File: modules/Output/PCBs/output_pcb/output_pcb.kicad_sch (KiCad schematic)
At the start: 12 parts, among them J10 Eurorack_2x5_Power, J11 Conn_01x03_Socket, J12 Conn_01x10_Socket, J3 ACJS-MV-3, J4 ACJS-MV-3, J5 ACJS-MV-3, J6 Conn_01x10_Pin, J7 Conn_01x10_Pin, J8 Conn_01x10_Pin, J9 Conn_01x10_Pin

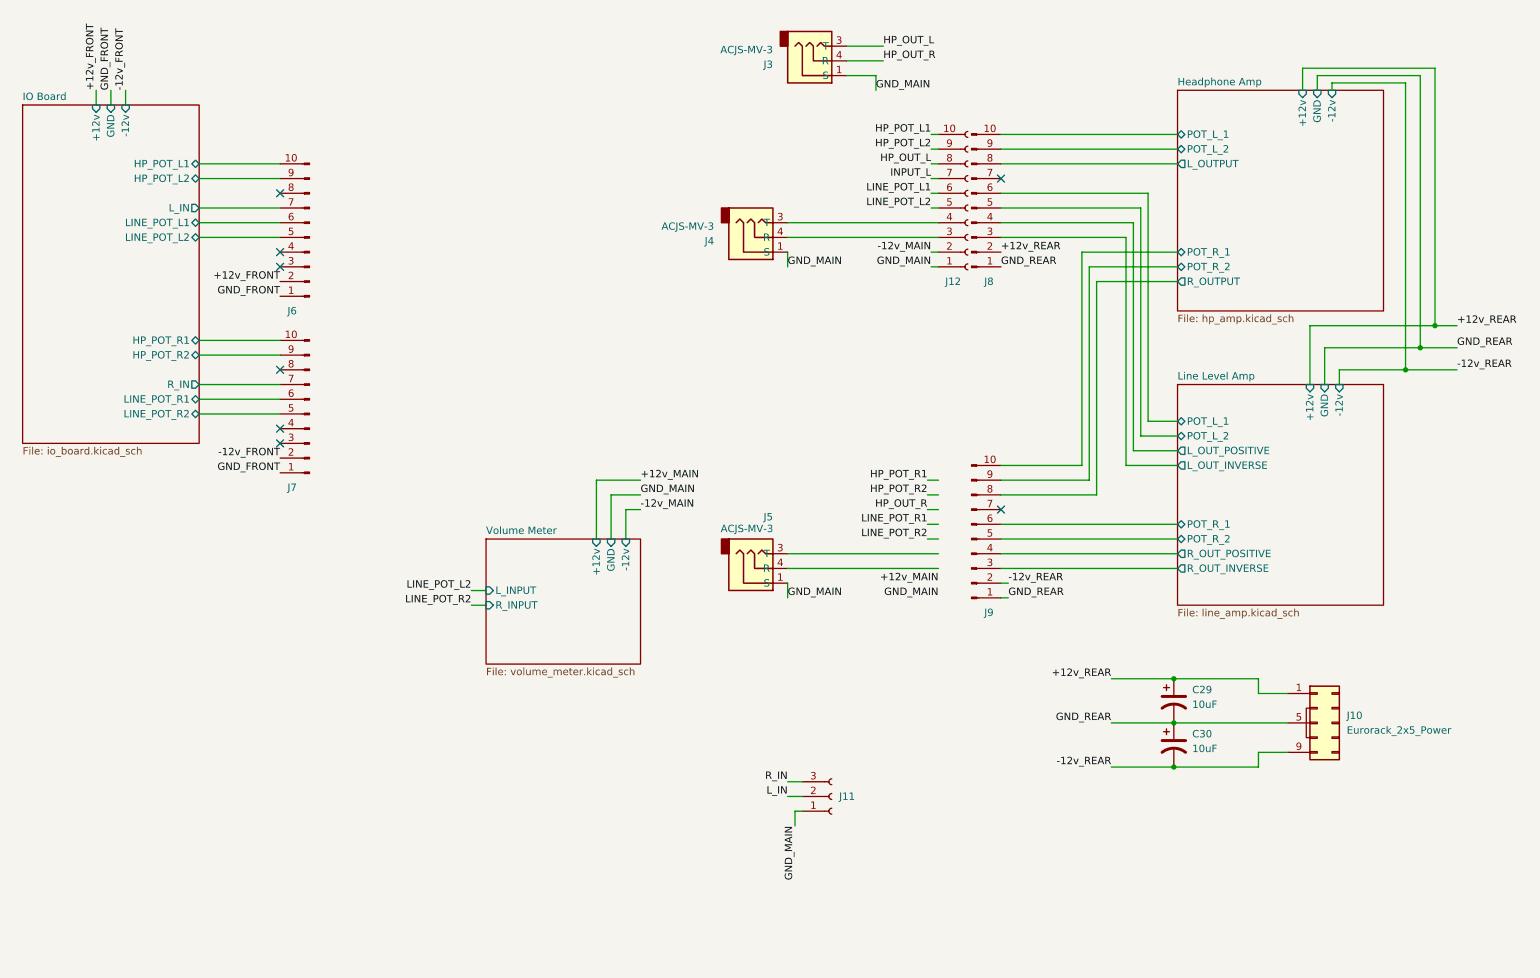
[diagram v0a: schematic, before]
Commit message: finish output PCB
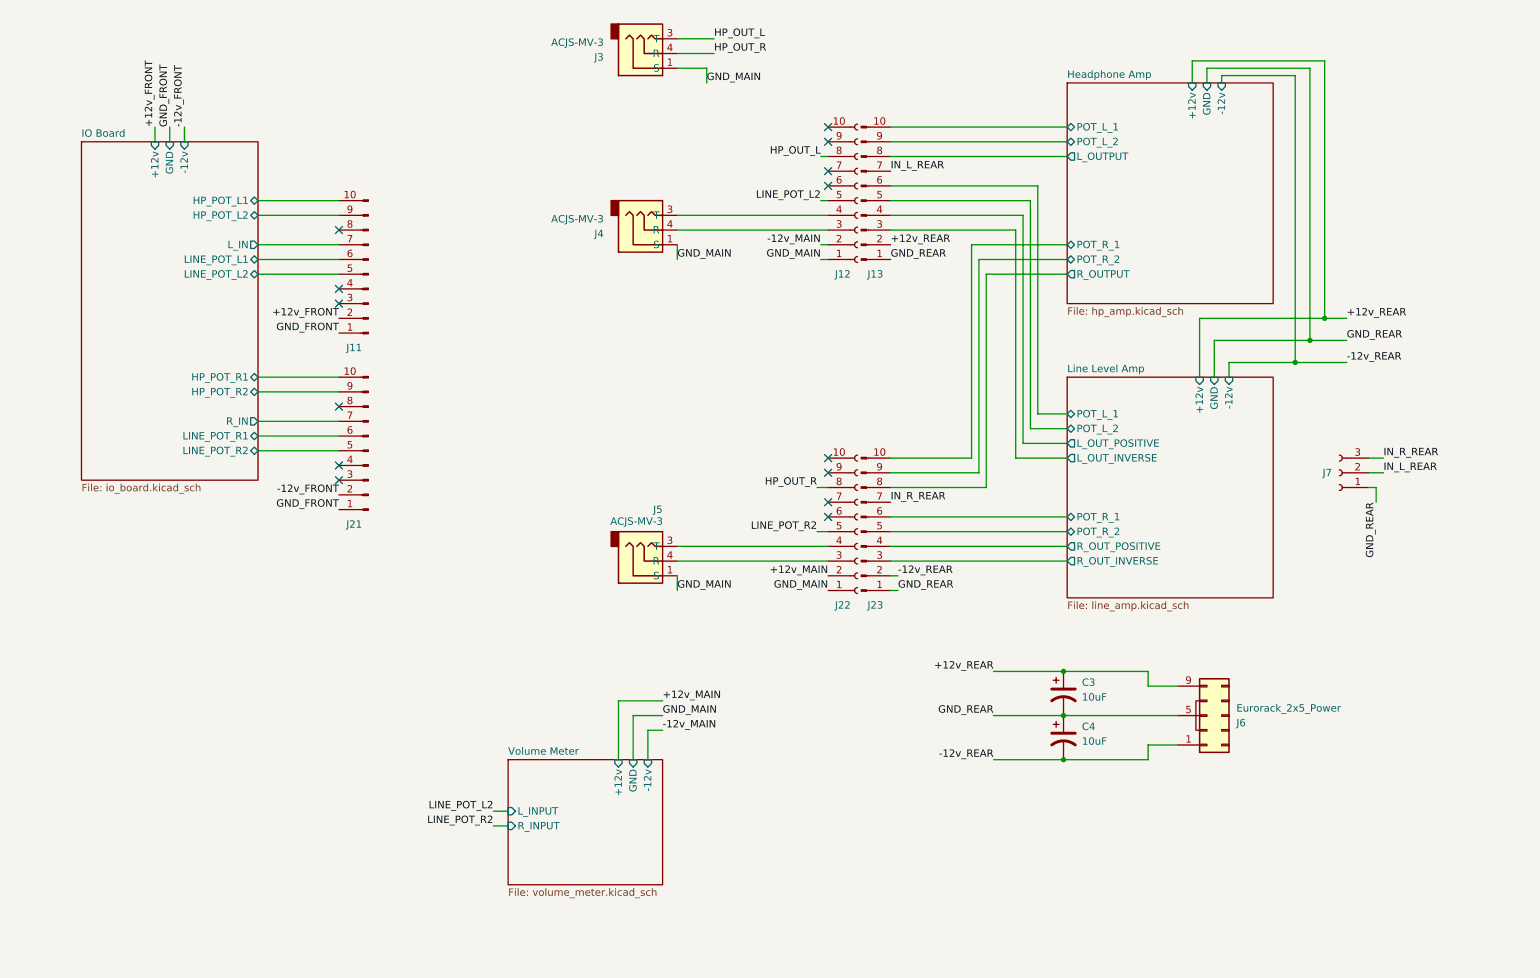
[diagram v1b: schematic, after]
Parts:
- added J22: Conn_01x10_Socket, Connector_PinHeader_2.54mm:PinHeader_1x10_P2.54mm_Vertical, symbol Connector:Conn_01x10_Socket
- J12: footprint (none) -> Connector_PinHeader_2.54mm:PinHeader_1x10_P2.54mm_Vertical
- J3, J4, J5: symbol Connector_Audio:AudioJack3 -> FreeModular:AudioJack_ACJS-MN-3
- renumbered C29 to C3, C30 to C4, J6 to J11, J8 to J13, J7 to J21, J9 to J23, J10 to J6, J11 to J7
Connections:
- net L_IN is gone; now on net IN_L_REAR: J7.2 (Pin_2)
- net R_IN is gone; now on net IN_R_REAR: J7.3 (Pin_3)
- net +12v_MAIN: now also J22.2 (Pin_2)
- net +12v_REAR: now also J6.10 (+12v), J6.9 (+12v); no longer J6.1 (-12v), J6.2 (-12v)
- net -12v_REAR: now also J6.1 (-12v), J6.2 (-12v); no longer J6.10 (+12v), J6.9 (+12v)
- net GND_MAIN: now also J22.1 (Pin_1); no longer J7.1 (Pin_1)
- net GND_REAR: now also J7.1 (Pin_1)
- net HP_OUT_R: now also J22.8 (Pin_8)
- net LINE_POT_R2: now also J22.5 (Pin_5)
- net IN_L_REAR: now reaches J13.7 (Pin_7)
- net IN_R_REAR: now reaches J23.7 (Pin_7)
- net at J5.3 (T): now also J22.4 (Pin_4)
- net at J5.4 (R): now also J22.3 (Pin_3)
- net HP_POT_L1: no longer names the net of J12.10 (Pin_10)
- net HP_POT_L2: no longer names the net of J12.9 (Pin_9)
- net INPUT_L: no longer names the net of J12.7 (Pin_7)
- net LINE_POT_L1: no longer names the net of J12.6 (Pin_6)
- no-connect marks 8 -> 14
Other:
- moved on the sheet: C3, C4, J11, J12, J13, J21, J23, J3, J4, J5, J6, J7

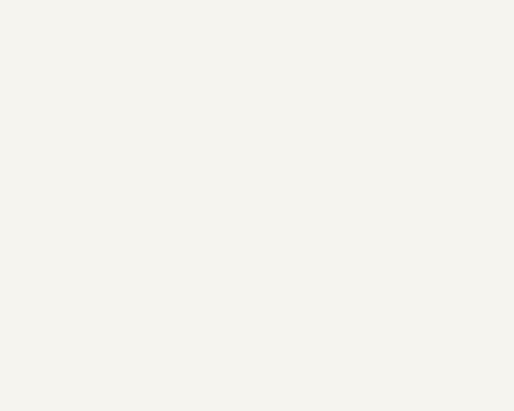
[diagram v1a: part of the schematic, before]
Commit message: revise output faceplate; add sifam knobs
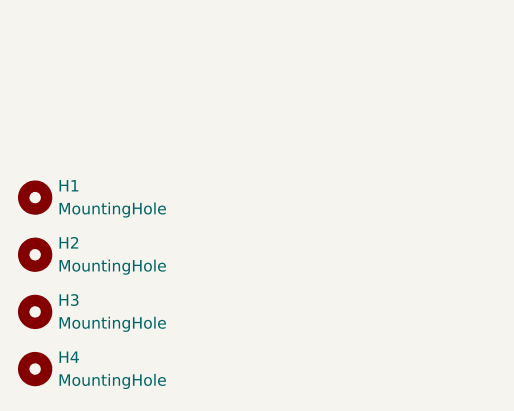
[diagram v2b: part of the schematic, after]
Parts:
- added H1, H2, H3, H4: MountingHole, MountingHole:MountingHole_2.7mm_M2.5, symbol Mechanical:MountingHole
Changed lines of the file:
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@@
+    )
+  )
+  (symbol (lib_id "Mechanical:MountingHole") (at 22.86 176.53 0) (unit 1)
+    (in_bom yes) (on_board yes) (dnp no) (fields_autoplaced)
+    (property "Reference" "H2" (at 25.4 175.26 0)
+      (effects (font (size 1.27 1.27)) (justify left))
+    )
+    (property "Value" "MountingHole" (at 25.4 177.8 0)
+      (effects (font (size 1.27 1.27)) (justify left))
+    )
+    (property "Footprint" "MountingHole:MountingHole_2.7mm_M2.5" (at 22.86 176.53 0)
+      (effects (font (size 1.27 1.27)) hide)
+    )
+    (property "Datasheet" "~" (at 22.86 176.53 0)
+      (effects (font (size 1.27 1.27)) hide)
+    )
+    (instances
+      (project "output_pcb"
+        (path "/9afe4d4d-3155-44ea-9484-068db54e495a"
+          (reference "H2") (unit 1)
+        )
+      )
+    )
+  )
+  (symbol (lib_id "Mechanical:MountingHole") (at 22.86 182.88 0) (unit 1)
+    (in_bom yes) (on_board yes) (dnp no) (fields_autoplaced)
+    (property "Reference" "H3" (at 25.4 181.61 0)
+      (effects (font (size 1.27 1.27)) (justify left))
+    )
+    (property "Value" "MountingHole" (at 25.4 184.15 0)
+      (effects (font (size 1.27 1.27)) (justify left))
+    )
+    (property "Footprint" "MountingHole:MountingHole_2.7mm_M2.5" (at 22.86 182.88 0)
+      (effects (font (size 1.27 1.27)) hide)
+    )
+    (property "Datasheet" "~" (at 22.86 182.88 0)
+      (effects (font (size 1.27 1.27)) hide)
+    )
+    (instances
+      (project "output_pcb"
+        (path "/9afe4d4d-3155-44ea-9484-068db54e495a"
+          (reference "H3") (unit 1)
+        )
+      )
     )
   )
@@
         (path "/9afe4d4d-3155-44ea-9484-068db54e495a"
           (reference "C4") (unit 1)
+        )
+      )
+    )
+  )
+  (symbol (lib_id "Mechanical:MountingHole") (at 22.86 170.18 0) (unit 1)
+    (in_bom yes) (on_board yes) (dnp no) (fields_autoplaced)
+    (property "Reference" "H1" (at 25.4 168.91 0)
+      (effects (font (size 1.27 1.27)) (justify left))
+    )
+    (property "Value" "MountingHole" (at 25.4 171.45 0)
+      (effects (font (size 1.27 1.27)) (justify left))
+    )
+    (property "Footprint" "MountingHole:MountingHole_2.7mm_M2.5" (at 22.86 170.18 0)
+      (effects (font (size 1.27 1.27)) hide)
+    )
+    (property "Datasheet" "~" (at 22.86 170.18 0)
+      (effects (font (size 1.27 1.27)) hide)
+    )
+    (instances
+      (project "output_pcb"
+        (path "/9afe4d4d-3155-44ea-9484-068db54e495a"
+          (reference "H1") (unit 1)
         )
       )
@@
         )
       )
+    )
+  )
+  (symbol (lib_id "Mechanical:MountingHole") (at 22.86 189.23 0) (unit 1)
+    (in_bom yes) (on_board yes) (dnp no) (fields_autoplaced)
+    (property "Reference" "H4" (at 25.4 187.96 0)
+      (effects (font (size 1.27 1.27)) (justify left))
+    )
+    (property "Value" "MountingHole" (at 25.4 190.5 0)
+      (effects (font (size 1.27 1.27)) (justify left))
+    )
+    (property "Footprint" "MountingHole:MountingHole_2.7mm_M2.5" (at 22.86 189.23 0)
+      (effects (font (size 1.27 1.27)) hide)
+    )
+    (property "Datasheet" "~" (at 22.86 189.23 0)
+      (effects (font (size 1.27 1.27)) hide)
+    )
+    (instances
+      (project "output_pcb"
+        (path "/9afe4d4d-3155-44ea-9484-068db54e495a"
+          (reference "H4") (unit 1)
+        )
+      )

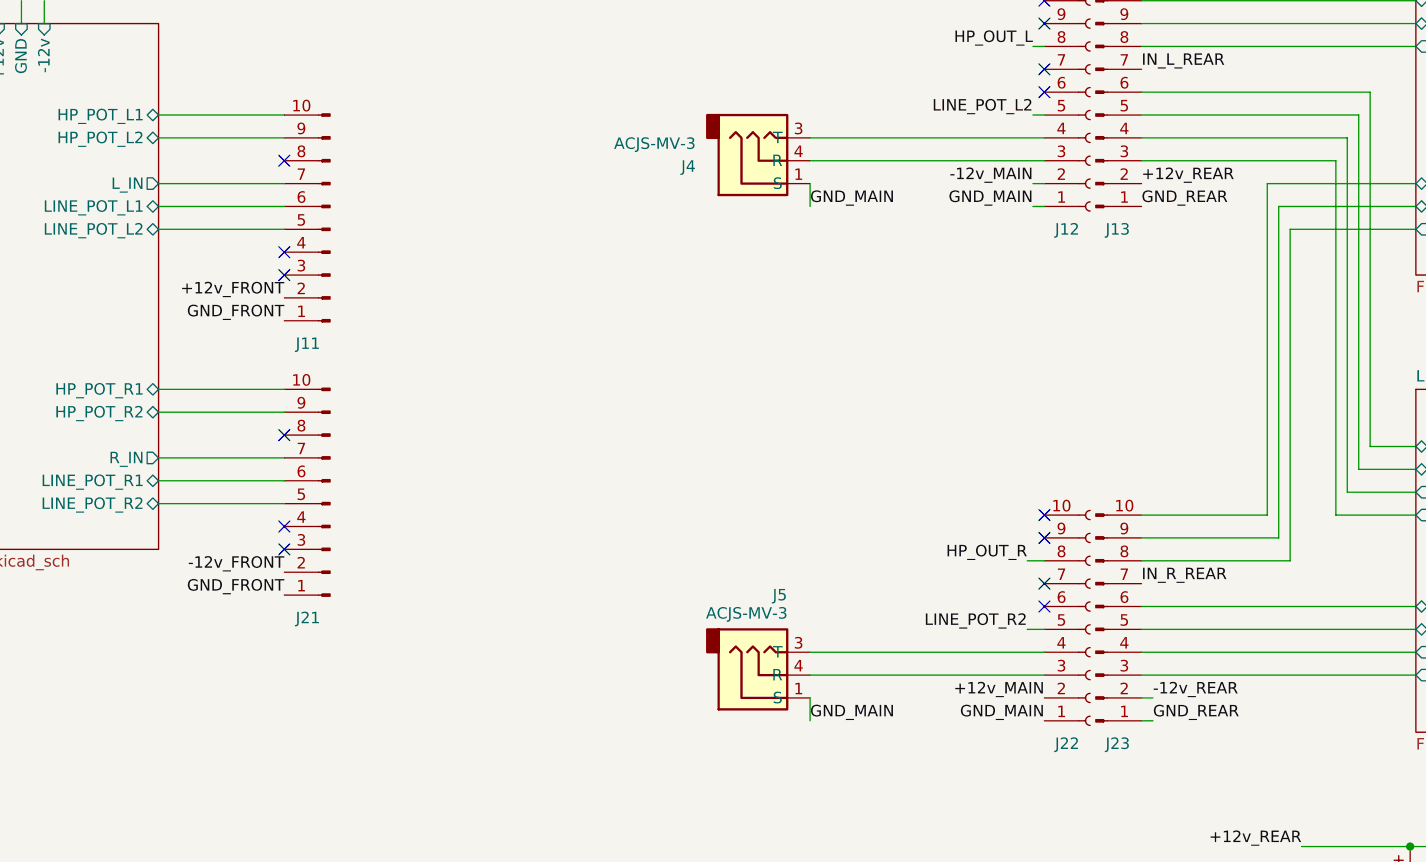
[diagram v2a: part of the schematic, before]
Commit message: fix polarity mismatch bugs in output pcb
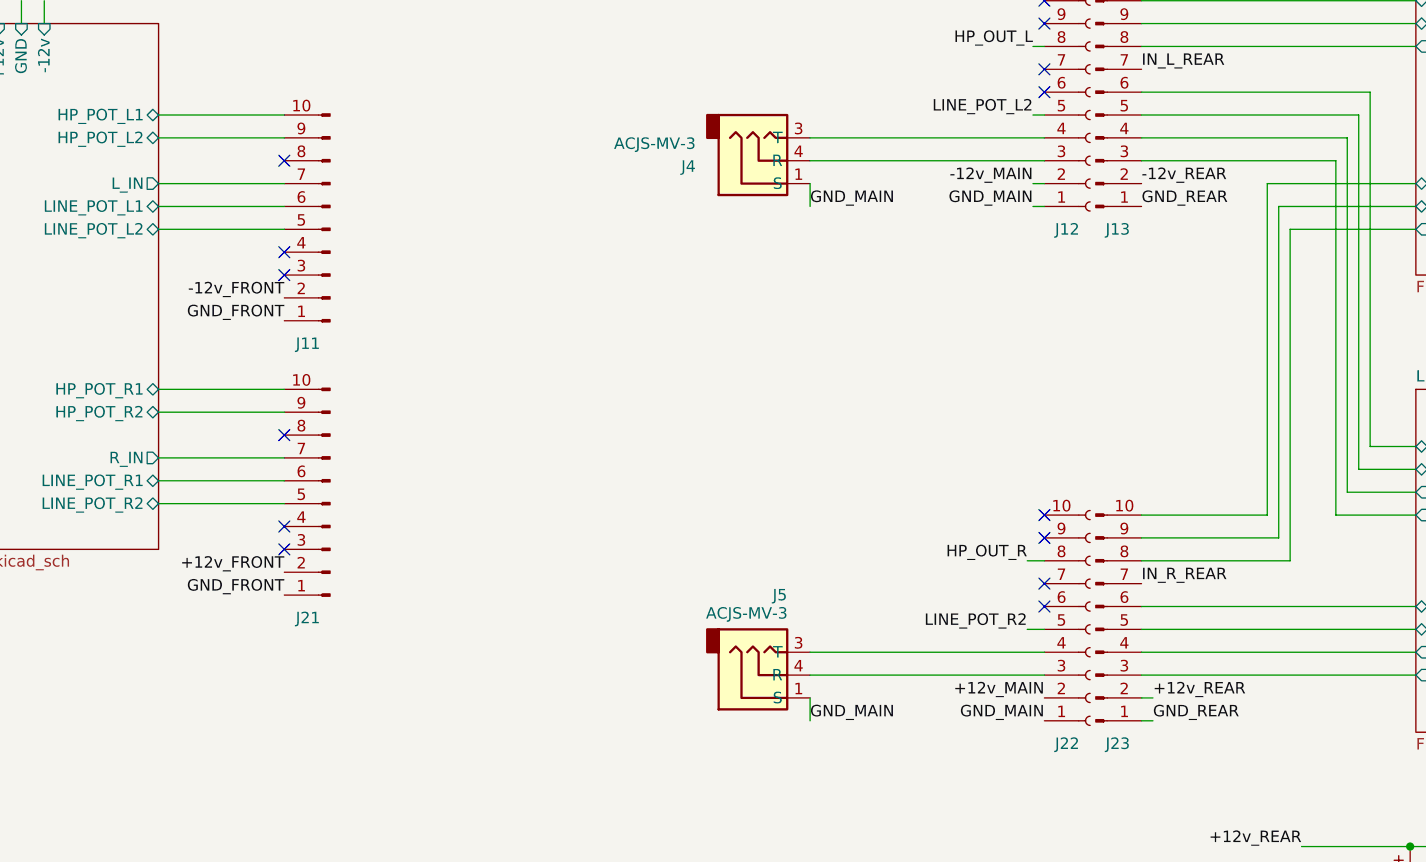
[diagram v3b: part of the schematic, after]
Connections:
- net +12v_FRONT: now also J21.2 (Pin_2); no longer J11.2 (Pin_2)
- net +12v_REAR: now also J23.2 (Pin_2); no longer J13.2 (Pin_2)
- net -12v_FRONT: now also J11.2 (Pin_2); no longer J21.2 (Pin_2)
- net -12v_REAR: now also J13.2 (Pin_2); no longer J23.2 (Pin_2)
